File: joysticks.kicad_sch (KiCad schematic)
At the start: 27 parts, among them J1 DB9_Male_MountingHoles, J2 DB9_Male_MountingHoles, J25 Joystick Ports Mezannine Lower, J26 Joystick Ports Mezannine Upper, SW1 SW_Push_DPDT, U10 74LS06N, U11 74LS06N, U5 74LS06N, U6 74LVC374, U7 74LVC374, U8 74LS374, U9 74LS374

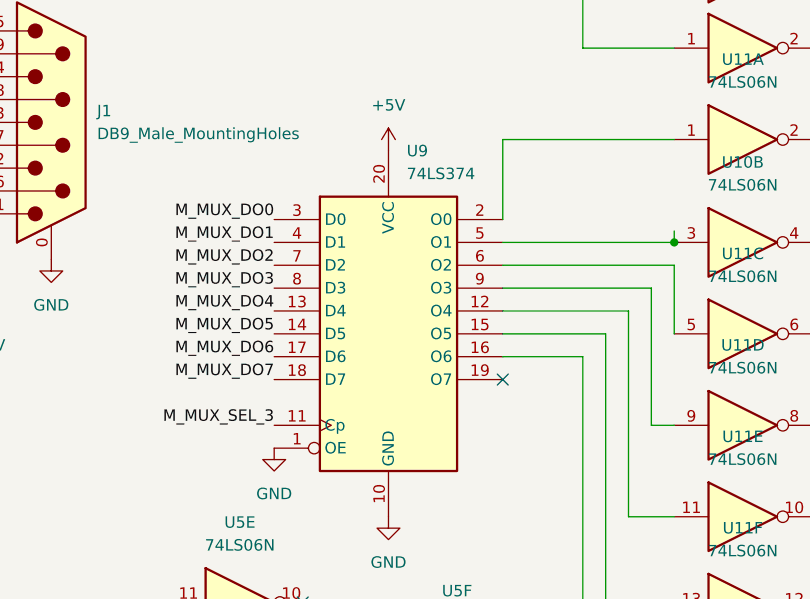
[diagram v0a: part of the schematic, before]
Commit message: make R/W signals on cart port open-collector with pullup #6
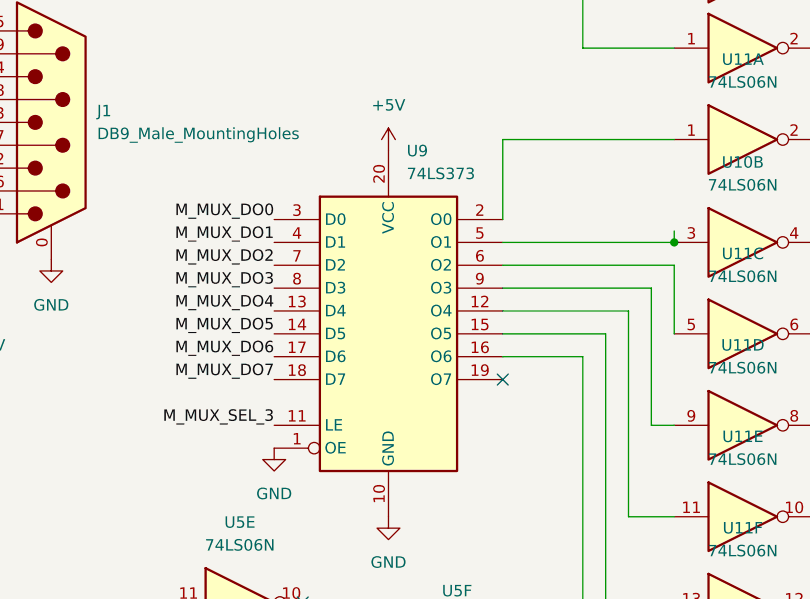
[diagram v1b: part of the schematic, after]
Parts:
- removed U9: 74LS374, Package_DIP:DIP-20_W7.62mm, symbol 74xx:74LS374
- added U9: 74LS373, Package_DIP:DIP-20_W7.62mm, symbol 74xx:74LS373
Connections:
- net +5V: now also U9.20 (VCC)
- net GND: now also U9.1 (OE), U9.10 (GND)
- net M_MUX_DO0: now also U9.3 (D0)
- net M_MUX_DO1: now also U9.4 (D1)
- net M_MUX_DO2: now also U9.7 (D2)
- net M_MUX_DO3: now also U9.8 (D3)
- net M_MUX_DO4: now also U9.13 (D4)
- net M_MUX_DO5: now also U9.14 (D5)
- net M_MUX_DO6: now also U9.17 (D6)
- net M_MUX_DO7: now also U9.18 (D7)
- net M_MUX_SEL_3: now also U9.11 (LE)
- net at U10.3: now also U9.5 (O1)
- net at U11.11: now also U9.12 (O4)
- net at U11.1: now also U9.2 (O0)
- net at U11.5: now also U9.6 (O2)
- net at U11.3: now also U9.16 (O6)
- net at U11.13: now also U9.15 (O5)
- net at U11.9: now also U9.9 (O3)
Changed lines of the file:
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@@
     (pin "2")
+  )
+  (symbol (lib_id "74xx:74LS373") (at 184.15 120.65 0) (unit 1)
+    (in_bom yes) (on_board yes) (fields_autoplaced)
+    (property "Reference" "U9" (id 0) (at 186.1694 100.33 0)
+      (effects (font (size 1.27 1.27)) (justify left))
+    )
+    (property "Value" "74LS373" (id 1) (at 186.1694 102.87 0)
+      (effects (font (size 1.27 1.27)) (justify left))
+    )
+    (property "Footprint" "Package_DIP:DIP-20_W7.62mm" (id 2) (at 184.15 120.65 0)
+      (effects (font (size 1.27 1.27)) hide)
+    )
+    (property "Datasheet" "http://www.ti.com/lit/gpn/sn74LS373" (id 3) (at 184.15 120.65 0)
+      (effects (font (size 1.27 1.27)) hide)
+    )
+    (pin "1")
+    (pin "10")
+    (pin "11")
+    (pin "12")
+    (pin "13")
+    (pin "14")
+    (pin "15")
+    (pin "16")
+    (pin "17")
+    (pin "18")
+    (pin "19")
+    (pin "2")
+    (pin "20")
+    (pin "3")
+    (pin "4")
+    (pin "5")
+    (pin "6")
+    (pin "7")
+    (pin "8")
+    (pin "9")
   )
   (symbol (lib_id "power:+5V") (at 252.095 41.91 90) (unit 1)
@@
     (pin "1")
   )
-  (symbol (lib_id "74xx:74LS374") (at 184.15 120.65 0) (unit 1)
-    (in_bom yes) (on_board yes) (fields_autoplaced)
-    (property "Reference" "U9" (id 0) (at 186.1694 100.33 0)
-      (effects (font (size 1.27 1.27)) (justify left))
-    )
-    (property "Value" "74LS374" (id 1) (at 186.1694 102.87 0)
-      (effects (font (size 1.27 1.27)) (justify left))
-    )
-    (property "Footprint" "Package_DIP:DIP-20_W7.62mm" (id 2) (at 184.15 120.65 0)
-      (effects (font (size 1.27 1.27)) hide)
-    )
-    (property "Datasheet" "http://www.ti.com/lit/gpn/sn74LS374" (id 3) (at 184.15 120.65 0)
-      (effects (font (size 1.27 1.27)) hide)
-    )
-    (pin "1")
-    (pin "10")
-    (pin "11")
-    (pin "12")
-    (pin "13")
-    (pin "14")
-    (pin "15")
-    (pin "16")
-    (pin "17")
-    (pin "18")
-    (pin "19")
-    (pin "2")
-    (pin "20")
-    (pin "3")
-    (pin "4")
-    (pin "5")
-    (pin "6")
-    (pin "7")
-    (pin "8")
-    (pin "9")
-  )
 )

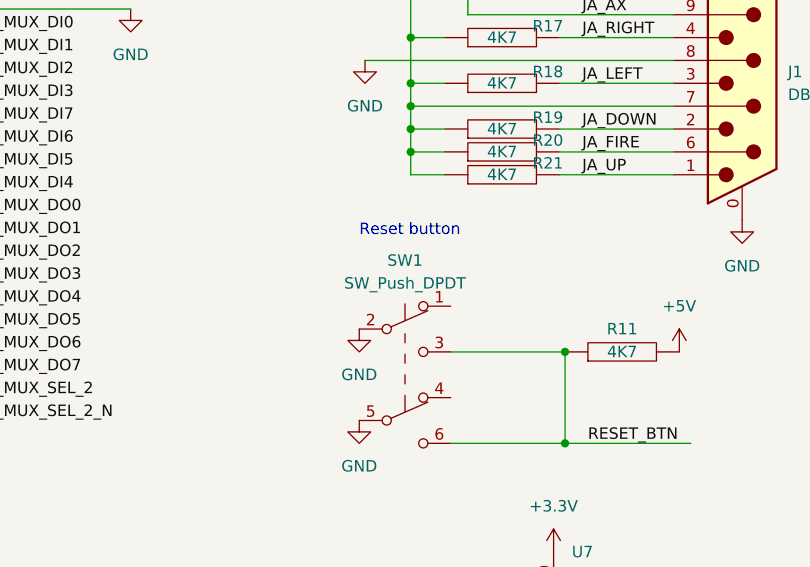
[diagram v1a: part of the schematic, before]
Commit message: place some mounting holes and reset button #3
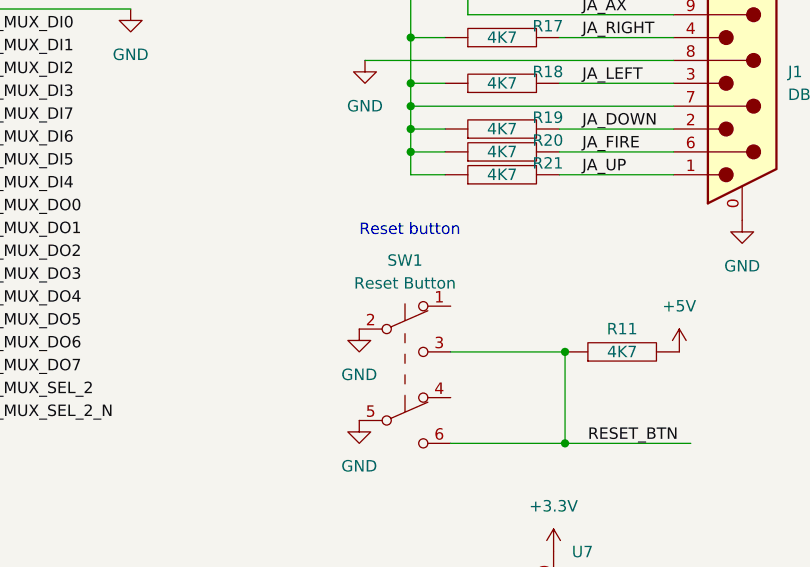
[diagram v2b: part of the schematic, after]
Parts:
- SW1: value SW_Push_DPDT -> Reset Button
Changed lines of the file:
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@@
     (in_bom yes) (on_board yes) (fields_autoplaced)
     (property "Reference" "SW1" (id 0) (at 109.22 116.84 0))
-    (property "Value" "SW_Push_DPDT" (id 1) (at 109.22 119.38 0))
+    (property "Value" "Reset Button" (id 1) (at 109.22 119.38 0))
     (property "Footprint" "snapeda:SPUJ191500" (id 2) (at 109.22 124.46 0)
       (effects (font (size 1.27 1.27)) hide)

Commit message: add missing footprints
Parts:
- R11: footprint Resistor_THT:R_Box_L8.4mm_W2.5mm_P5.08mm -> snapeda:Labeled Resistor
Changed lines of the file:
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@@
     (property "Reference" "R11" (id 0) (at 133.35 124.46 90))
     (property "Value" "4K7" (id 1) (at 133.35 127 90))
-    (property "Footprint" "Resistor_THT:R_Box_L8.4mm_W2.5mm_P5.08mm" (id 2) (at 133.35 127 0)
+    (property "Footprint" "snapeda:Labeled Resistor" (id 2) (at 133.35 127 0)
       (effects (font (size 1.27 1.27)) hide)
     )

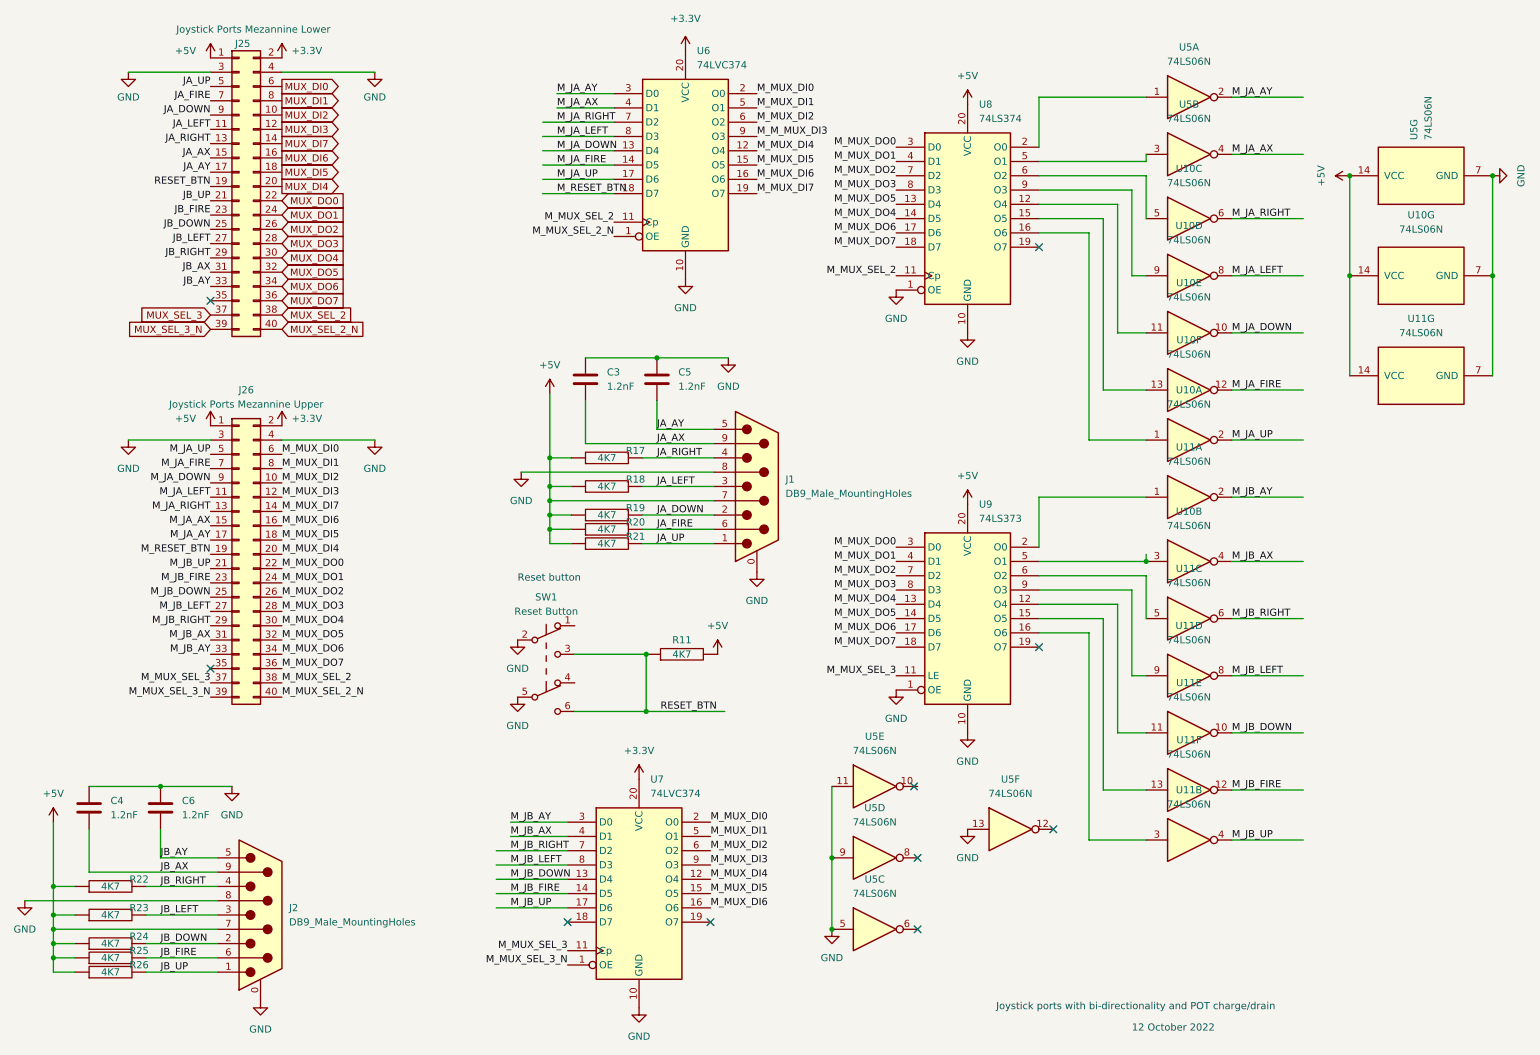
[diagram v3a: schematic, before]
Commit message: renumber MUX registers to ease routing
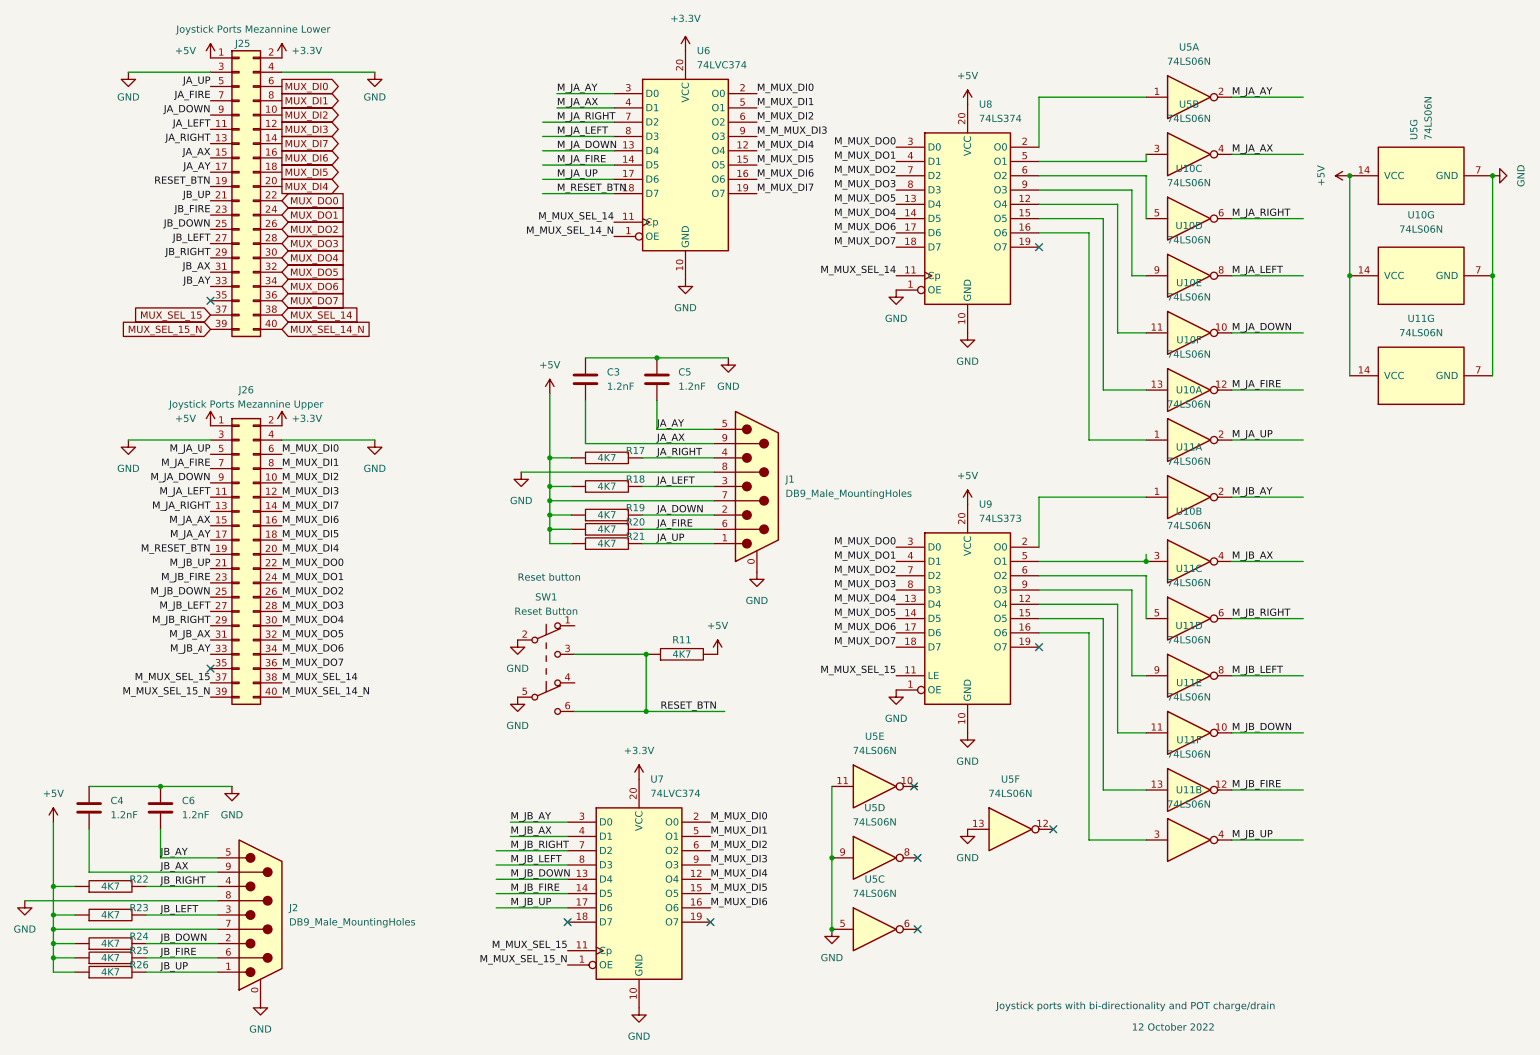
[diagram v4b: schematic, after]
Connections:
- net MUX_SEL_2 renamed MUX_SEL_14
- net MUX_SEL_2_N renamed MUX_SEL_14_N
- net MUX_SEL_3 renamed MUX_SEL_15
- net MUX_SEL_3_N renamed MUX_SEL_15_N
- net M_MUX_SEL_2 renamed M_MUX_SEL_14
- net M_MUX_SEL_2_N renamed M_MUX_SEL_14_N
- net M_MUX_SEL_3 renamed M_MUX_SEL_15
- net M_MUX_SEL_3_N renamed M_MUX_SEL_15_N
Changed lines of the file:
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@@
     (effects (font (size 1.27 1.27)) (justify right bottom))
   )
-  (label "M_MUX_SEL_3" (at 49.53 132.08 180)
+  (label "M_MUX_SEL_15" (at 49.53 132.08 180)
     (effects (font (size 1.27 1.27)) (justify right bottom))
   )
@@
     (effects (font (size 1.27 1.27)) (justify right bottom))
   )
-  (label "M_MUX_SEL_3_N" (at 49.53 134.62 180)
+  (label "M_MUX_SEL_15_N" (at 49.53 134.62 180)
     (effects (font (size 1.27 1.27)) (justify right bottom))
   )
@@
     (effects (font (size 1.27 1.27)) (justify left bottom))
   )
-  (label "M_MUX_SEL_3_N" (at 113.03 182.245 180)
+  (label "M_MUX_SEL_15_N" (at 113.03 182.245 180)
     (effects (font (size 1.27 1.27)) (justify right bottom))
   )
@@
     (effects (font (size 1.27 1.27)) (justify left bottom))
   )
-  (label "M_MUX_SEL_2" (at 171.45 59.69 180)
+  (label "M_MUX_SEL_14" (at 171.45 59.69 180)
     (effects (font (size 1.27 1.27)) (justify right bottom))
   )
@@
     (effects (font (size 1.27 1.27)) (justify left bottom))
   )
-  (label "M_MUX_SEL_2_N" (at 121.285 52.705 180)
+  (label "M_MUX_SEL_14_N" (at 121.285 52.705 180)
     (effects (font (size 1.27 1.27)) (justify right bottom))
   )
@@
     (effects (font (size 1.27 1.27)) (justify left bottom))
   )
-  (label "M_MUX_SEL_3" (at 171.45 130.81 180)
+  (label "M_MUX_SEL_15" (at 171.45 130.81 180)
     (effects (font (size 1.27 1.27)) (justify right bottom))
   )
@@
     (effects (font (size 1.27 1.27)) (justify left bottom))
   )
-  (label "M_MUX_SEL_3" (at 113.03 179.705 180)
+  (label "M_MUX_SEL_15" (at 113.03 179.705 180)
     (effects (font (size 1.27 1.27)) (justify right bottom))
   )
@@
     (effects (font (size 1.27 1.27)) (justify left bottom))
   )
-  (label "M_MUX_SEL_2" (at 121.285 50.165 180)
+  (label "M_MUX_SEL_14" (at 121.285 50.165 180)
     (effects (font (size 1.27 1.27)) (justify right bottom))
   )
@@
     (effects (font (size 1.27 1.27)) (justify left bottom))
   )
-  (label "M_MUX_SEL_2" (at 62.23 132.08 0)
+  (label "M_MUX_SEL_14" (at 62.23 132.08 0)
     (effects (font (size 1.27 1.27)) (justify left bottom))
   )
@@
     (effects (font (size 1.27 1.27)) (justify left bottom))
   )
-  (label "M_MUX_SEL_2_N" (at 62.23 134.62 0)
+  (label "M_MUX_SEL_14_N" (at 62.23 134.62 0)
     (effects (font (size 1.27 1.27)) (justify left bottom))
   )
@@
     )
   )
-  (global_label "MUX_SEL_3_N" (shape input) (at 49.53 69.215 180) (fields_autoplaced)
+  (global_label "MUX_SEL_15_N" (shape input) (at 49.53 69.215 180) (fields_autoplaced)
     (effects (font (size 1.27 1.27)) (justify right))
-    (property "Intersheet References" "${INTERSHEET_REFS}" (id 0) (at 34.2959 69.1356 0)
+    (property "Intersheet References" "${INTERSHEET_REFS}" (id 0) (at 33.0864 69.1356 0)
       (effects (font (size 1.27 1.27)) (justify right) hide)
     )
@@
     )
   )
-  (global_label "MUX_SEL_2_N" (shape input) (at 62.23 69.215 0) (fields_autoplaced)
-    (effects (font (size 1.27 1.27)) (justify left))
-    (property "Intersheet References" "${INTERSHEET_REFS}" (id 0) (at 77.4641 69.1356 0)
-      (effects (font (size 1.27 1.27)) (justify left) hide)
-    )
-  )
-  (global_label "MUX_SEL_3" (shape input) (at 49.53 66.675 180) (fields_autoplaced)
+  (global_label "MUX_SEL_14_N" (shape input) (at 62.23 69.215 0) (fields_autoplaced)
+    (effects (font (size 1.27 1.27)) (justify left))
+    (property "Intersheet References" "${INTERSHEET_REFS}" (id 0) (at 78.6736 69.1356 0)
+      (effects (font (size 1.27 1.27)) (justify left) hide)
+    )
+  )
+  (global_label "MUX_SEL_15" (shape input) (at 49.53 66.675 180) (fields_autoplaced)
     (effects (font (size 1.27 1.27)) (justify right))
-    (property "Intersheet References" "${INTERSHEET_REFS}" (id 0) (at 36.594 66.5956 0)
+    (property "Intersheet References" "${INTERSHEET_REFS}" (id 0) (at 35.3845 66.5956 0)
       (effects (font (size 1.27 1.27)) (justify right) hide)
     )
@@
     )
   )
-  (global_label "MUX_SEL_2" (shape input) (at 62.23 66.675 0) (fields_autoplaced)
-    (effects (font (size 1.27 1.27)) (justify left))
-    (property "Intersheet References" "${INTERSHEET_REFS}" (id 0) (at 75.166 66.5956 0)
-      (effects (font (size 1.27 1.27)) (justify left) hide)
-    )
+  (global_label "MUX_SEL_14" (shape input) (at 62.23 66.675 0) (fields_autoplaced)
+    (effects (font (size 1.27 1.27)) (justify left))
+    (property "Intersheet References" "${INTERSHEET_REFS}" (id 0) (at 76.3755 66.5956 0)
+      (effects (font (size 1.27 1.27)) (justify left) hide)
+    )
